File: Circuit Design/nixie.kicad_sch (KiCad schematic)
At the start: 0 parts

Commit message: all the routing is done
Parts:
- added C1, C10, C11, C12, C2, C3, C34, C35, C36, C37, C4, C5, C6, C7, C8, C9: 1uF, CoF_Capacitor:C-0402, symbol CoE_Capacitor:1uF
- added CP1, CP10, CP100, CP101, CP102, CP103, CP104, CP105, CP106, CP107, CP108, CP109, CP11, CP110, CP111, CP112, CP113, CP114, CP115, CP116, CP117, CP118, CP119, CP12, CP120, CP121, CP122, CP123, CP124, CP125, CP126, CP127, CP128, CP129, CP13, CP130, CP131, CP132, CP133, CP134, CP135, CP136, CP137, CP138, CP139, CP14, CP140, CP141, CP142, CP143, CP144, CP145, CP146, CP147, CP148, CP149, CP15, CP150, CP151, CP152, CP153, CP154, CP155, CP156, CP157, CP158, CP159, CP16, CP160, CP161, CP162, CP163, CP164, CP165, CP166, CP167, CP168, CP169, CP17, CP170, CP171, CP172, CP173, CP174, CP175, CP176, CP177, CP178, CP179, CP18, CP180, CP181, CP182, CP183, CP184, CP185, CP186, CP187, CP188, CP189, CP19, CP190, CP191, CP192, CP193, CP194, CP195, CP196, CP197, CP198, CP199, CP2, CP20, CP200, CP201, CP202, CP203, CP204, CP205, CP206, CP207, CP208, CP209, CP21, CP210, CP211, CP212, CP213, CP214, CP215, CP216, CP217, CP218, CP219, CP22, CP220, CP221, CP222, CP223, CP224, CP225, CP226, CP227, CP228, CP229, CP23, CP230, CP231, CP232, CP24, CP25, CP26, CP27, CP28, CP29, CP3, CP30, CP31, CP32, CP33, CP34, CP35, CP36, CP37, CP38, CP39, CP4, CP40, CP41, CP42, CP43, CP44, CP45, CP46, CP47, CP48, CP49, CP5, CP50, CP51, CP52, CP53, CP54, CP55, CP56, CP57, CP58, CP59, CP6, CP60, CP61, CP62, CP63, CP64, CP65, CP66, CP67, CP68, CP69, CP7, CP70, CP71, CP72, CP73, CP74, CP75, CP76, CP77, CP78, CP79, CP8, CP80, CP81, CP82, CP83, CP84, CP85, CP86, CP87, CP88, CP89, CP9, CP90, CP91, CP92, CP93, CP94, CP95, CP96, CP97, CP98, CP99: SolderPad, CoF_Connector:SolderPt_1x2mm, symbol Connector:TestPoint
- added J1: BM04B-GHS-TBT, CoF_Connector:BM04B-GHS-TBT, symbol CoE_Connector:BM04B-GHS-TBT
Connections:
- net LED Driver/CS1: now also CP169.1
- net LED Driver/CS10: now also CP115.1
- net LED Driver/CS11: now also CP109.1
- net LED Driver/CS12: now also CP103.1
- net LED Driver/CS13: now also CP97.1
- net LED Driver/CS14: now also CP91.1
- net LED Driver/CS15: now also CP85.1
- net LED Driver/CS16: now also CP79.1
- net LED Driver/CS17: now also CP73.1
- net LED Driver/CS18: now also CP67.1
- net LED Driver/CS2: now also CP163.1
- net LED Driver/CS3: now also CP157.1
- net LED Driver/CS4: now also CP151.1
- net LED Driver/CS5: now also CP145.1
- net LED Driver/CS6: now also CP139.1
- net LED Driver/CS7: now also CP133.1
- net LED Driver/CS8: now also CP127.1
- net LED Driver/CS9: now also CP121.1
- net LED Driver/SW1: now also CP1.1
- net LED Driver/SW10: now also CP55.1
- net LED Driver/SW11: now also CP61.1
- net LED Driver/SW2: now also CP7.1
- net LED Driver/SW3: now also CP13.1
- net LED Driver/SW4: now also CP19.1
- net LED Driver/SW5: now also CP25.1
- net LED Driver/SW6: now also CP31.1
- net LED Driver/SW7: now also CP37.1
- net LED Driver/SW8: now also CP43.1
- net LED Driver/SW9: now also CP49.1
- net Screen/CS1: now also CP170.1
- net Screen/CS10: now also CP116.1
- net Screen/CS11: now also CP110.1
- net Screen/CS12: now also CP104.1
- net Screen/CS13: now also CP98.1
- net Screen/CS14: now also CP92.1
- net Screen/CS15: now also CP86.1
- net Screen/CS16: now also CP80.1
- net Screen/CS17: now also CP74.1
- net Screen/CS18: now also CP68.1
- net Screen/CS2: now also CP164.1
- net Screen/CS3: now also CP158.1
- net Screen/CS4: now also CP152.1
- net Screen/CS5: now also CP146.1
- net Screen/CS6: now also CP140.1
- net Screen/CS7: now also CP134.1
- net Screen/CS8: now also CP128.1
- net Screen/CS9: now also CP122.1
- net Screen/SW1: now also CP62.1
- net Screen/SW10: now also CP8.1
- net Screen/SW11: now also CP2.1
- net Screen/SW2: now also CP56.1
- net Screen/SW3: now also CP50.1
- net Screen/SW4: now also CP44.1
- net Screen/SW5: now also CP38.1
- net Screen/SW6: now also CP32.1
- net Screen/SW7: now also CP26.1
- net Screen/SW8: now also CP20.1
- net Screen/SW9: now also CP14.1
- new net +3V3: C1.1, C10.1, C11.1, C12.1, C2.1, C3.1, C34.1, C35.1, C36.1, C37.1, C4.1, C5.1, C6.1, C7.1, C8.1, C9.1, J1.1 (Pin_1)
- new net GND: C1.2, C10.2, C11.2, C12.2, C2.2, C3.2, C34.2, C35.2, C36.2, C37.2, C4.2, C5.2, C6.2, C7.2, C8.2, C9.2, J1.4 (Pin_4), J1.MP (MountPin)
- new net LED Driver1/CS1: CP171.1
- new net LED Driver1/CS10: CP117.1
- new net LED Driver1/CS11: CP111.1
- new net LED Driver1/CS12: CP105.1
- new net LED Driver1/CS13: CP99.1
- new net LED Driver1/CS14: CP93.1
- new net LED Driver1/CS15: CP87.1
- new net LED Driver1/CS16: CP81.1
- new net LED Driver1/CS17: CP75.1
- new net LED Driver1/CS18: CP69.1
- new net LED Driver1/CS2: CP165.1
- new net LED Driver1/CS3: CP159.1
- new net LED Driver1/CS4: CP153.1
- new net LED Driver1/CS5: CP147.1
- new net LED Driver1/CS6: CP141.1
- new net LED Driver1/CS7: CP135.1
- new net LED Driver1/CS8: CP129.1
- new net LED Driver1/CS9: CP123.1
- new net LED Driver1/SW1: CP3.1
- new net LED Driver1/SW10: CP57.1
- new net LED Driver1/SW11: CP63.1
- new net LED Driver1/SW2: CP9.1
- new net LED Driver1/SW3: CP15.1
- new net LED Driver1/SW4: CP21.1
- new net LED Driver1/SW5: CP27.1
- new net LED Driver1/SW6: CP33.1
- new net LED Driver1/SW7: CP39.1
- new net LED Driver1/SW8: CP45.1
- new net LED Driver1/SW9: CP51.1
- new net LED Driver2/CS1: CP173.1
- new net LED Driver2/CS10: CP119.1
- new net LED Driver2/CS11: CP113.1
- new net LED Driver2/CS12: CP107.1
- new net LED Driver2/CS13: CP101.1
- new net LED Driver2/CS14: CP95.1
- new net LED Driver2/CS15: CP89.1
- new net LED Driver2/CS16: CP83.1
- new net LED Driver2/CS17: CP77.1
- new net LED Driver2/CS18: CP71.1
- new net LED Driver2/CS2: CP167.1
- new net LED Driver2/CS3: CP161.1
- new net LED Driver2/CS4: CP155.1
- new net LED Driver2/CS5: CP149.1
- new net LED Driver2/CS6: CP143.1
- new net LED Driver2/CS7: CP137.1
- new net LED Driver2/CS8: CP131.1
- new net LED Driver2/CS9: CP125.1
- new net LED Driver2/SW1: CP5.1
- new net LED Driver2/SW10: CP59.1
- new net LED Driver2/SW11: CP65.1
- new net LED Driver2/SW2: CP11.1
- new net LED Driver2/SW3: CP17.1
- new net LED Driver2/SW4: CP23.1
- new net LED Driver2/SW5: CP29.1
- new net LED Driver2/SW6: CP35.1
- new net LED Driver2/SW7: CP41.1
- new net LED Driver2/SW8: CP47.1
- new net LED Driver2/SW9: CP53.1
- new net LED Driver3/CS1: CP231.1
- new net LED Driver3/CS10: CP213.1
- new net LED Driver3/CS11: CP211.1
- new net LED Driver3/CS12: CP209.1
- new net LED Driver3/CS13: CP207.1
- new net LED Driver3/CS14: CP205.1
- new net LED Driver3/CS15: CP203.1
- new net LED Driver3/CS16: CP201.1
- new net LED Driver3/CS17: CP199.1
- new net LED Driver3/CS18: CP197.1
- new net LED Driver3/CS2: CP229.1
- new net LED Driver3/CS3: CP227.1
- new net LED Driver3/CS4: CP225.1
- new net LED Driver3/CS5: CP223.1
- new net LED Driver3/CS6: CP221.1
- new net LED Driver3/CS7: CP219.1
- new net LED Driver3/CS8: CP217.1
- new net LED Driver3/CS9: CP215.1
- new net LED Driver3/SW1: CP175.1
- new net LED Driver3/SW10: CP193.1
- new net LED Driver3/SW11: CP195.1
- new net LED Driver3/SW2: CP177.1
- new net LED Driver3/SW3: CP179.1
- new net LED Driver3/SW4: CP181.1
- new net LED Driver3/SW5: CP183.1
- new net LED Driver3/SW6: CP185.1
- new net LED Driver3/SW7: CP187.1
- new net LED Driver3/SW8: CP189.1
- new net LED Driver3/SW9: CP191.1
- new net SCL: J1.2 (Pin_2)
- new net SDA: J1.3 (Pin_3)
- new net Screen1/CS1: CP172.1
- new net Screen1/CS10: CP118.1
- new net Screen1/CS11: CP112.1
- new net Screen1/CS12: CP106.1
- new net Screen1/CS13: CP100.1
- new net Screen1/CS14: CP94.1
- new net Screen1/CS15: CP88.1
- new net Screen1/CS16: CP82.1
- new net Screen1/CS17: CP76.1
- new net Screen1/CS18: CP70.1
- new net Screen1/CS2: CP166.1
- new net Screen1/CS3: CP160.1
- new net Screen1/CS4: CP154.1
- new net Screen1/CS5: CP148.1
- new net Screen1/CS6: CP142.1
- new net Screen1/CS7: CP136.1
- new net Screen1/CS8: CP130.1
- new net Screen1/CS9: CP124.1
- new net Screen1/SW1: CP64.1
- new net Screen1/SW10: CP10.1
- new net Screen1/SW11: CP4.1
- new net Screen1/SW2: CP58.1
- new net Screen1/SW3: CP52.1
- new net Screen1/SW4: CP46.1
- new net Screen1/SW5: CP40.1
- new net Screen1/SW6: CP34.1
- new net Screen1/SW7: CP28.1
- new net Screen1/SW8: CP22.1
- new net Screen1/SW9: CP16.1
- new net Screen2/CS1: CP174.1
- new net Screen2/CS10: CP120.1
- new net Screen2/CS11: CP114.1
- new net Screen2/CS12: CP108.1
- new net Screen2/CS13: CP102.1
- new net Screen2/CS14: CP96.1
- new net Screen2/CS15: CP90.1
- new net Screen2/CS16: CP84.1
- new net Screen2/CS17: CP78.1
- new net Screen2/CS18: CP72.1
- new net Screen2/CS2: CP168.1
- new net Screen2/CS3: CP162.1
- new net Screen2/CS4: CP156.1
- new net Screen2/CS5: CP150.1
- new net Screen2/CS6: CP144.1
- new net Screen2/CS7: CP138.1
- new net Screen2/CS8: CP132.1
- new net Screen2/CS9: CP126.1
- new net Screen2/SW1: CP66.1
- new net Screen2/SW10: CP12.1
- new net Screen2/SW11: CP6.1
- new net Screen2/SW2: CP60.1
- new net Screen2/SW3: CP54.1
- new net Screen2/SW4: CP48.1
- new net Screen2/SW5: CP42.1
- new net Screen2/SW6: CP36.1
- new net Screen2/SW7: CP30.1
- new net Screen2/SW8: CP24.1
- new net Screen2/SW9: CP18.1
- new net Screen3/CS1: CP232.1
- new net Screen3/CS10: CP214.1
- new net Screen3/CS11: CP212.1
- new net Screen3/CS12: CP210.1
- new net Screen3/CS13: CP208.1
- new net Screen3/CS14: CP206.1
- new net Screen3/CS15: CP204.1
- new net Screen3/CS16: CP202.1
- new net Screen3/CS17: CP200.1
- new net Screen3/CS18: CP198.1
- new net Screen3/CS2: CP230.1
- new net Screen3/CS3: CP228.1
- new net Screen3/CS4: CP226.1
- new net Screen3/CS5: CP224.1
- new net Screen3/CS6: CP222.1
- new net Screen3/CS7: CP220.1
- new net Screen3/CS8: CP218.1
- new net Screen3/CS9: CP216.1
- new net Screen3/SW1: CP196.1
- new net Screen3/SW10: CP178.1
- new net Screen3/SW11: CP176.1
- new net Screen3/SW2: CP194.1
- new net Screen3/SW3: CP192.1
- new net Screen3/SW4: CP190.1
- new net Screen3/SW5: CP188.1
- new net Screen3/SW6: CP186.1
- new net Screen3/SW7: CP184.1
- new net Screen3/SW8: CP182.1
- new net Screen3/SW9: CP180.1
- no-connect marks 0 -> 4
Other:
- added sheet LED Driver1 (controller.kicad_sch)
- added sheet LED Driver2 (controller.kicad_sch)
- added sheet LED Driver3 (controller.kicad_sch)
- added sheet Screen1 (matrix.kicad_sch)
- added sheet Screen2 (matrix.kicad_sch)
- added sheet Screen3 (matrix.kicad_sch)
- sheet LED Driver ports: added ADDR1, ADDR2, SCL, SDA, SDB, SYNC; removed none

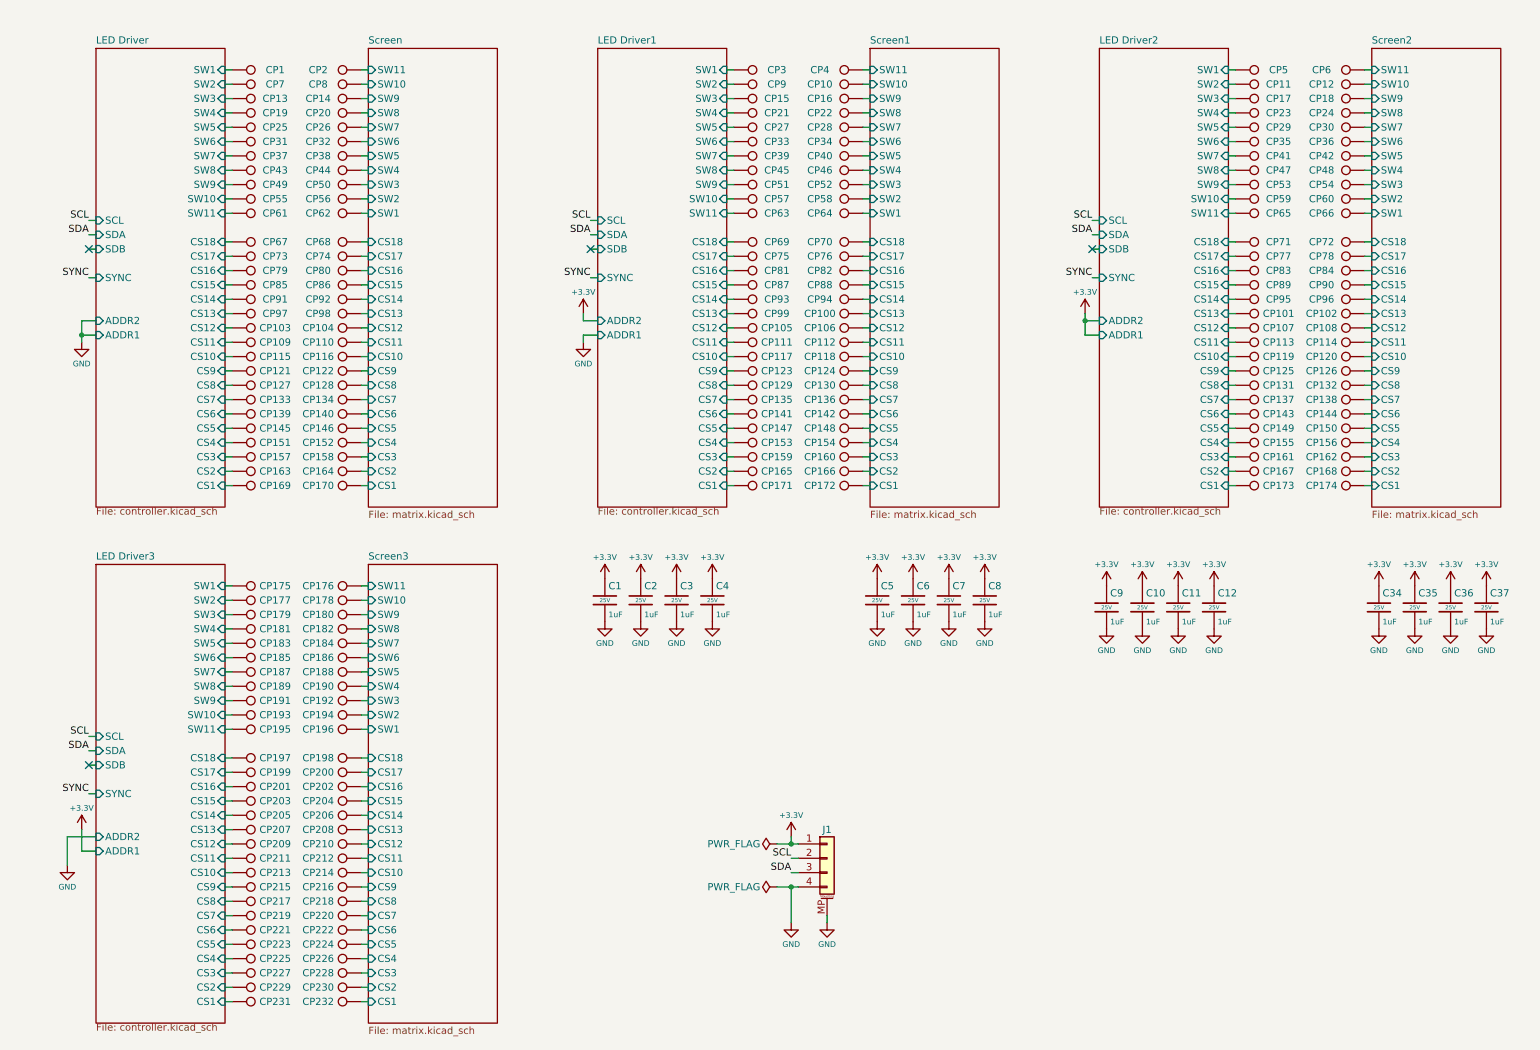
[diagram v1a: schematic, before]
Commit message: added IS31FL3731 and, edited its page
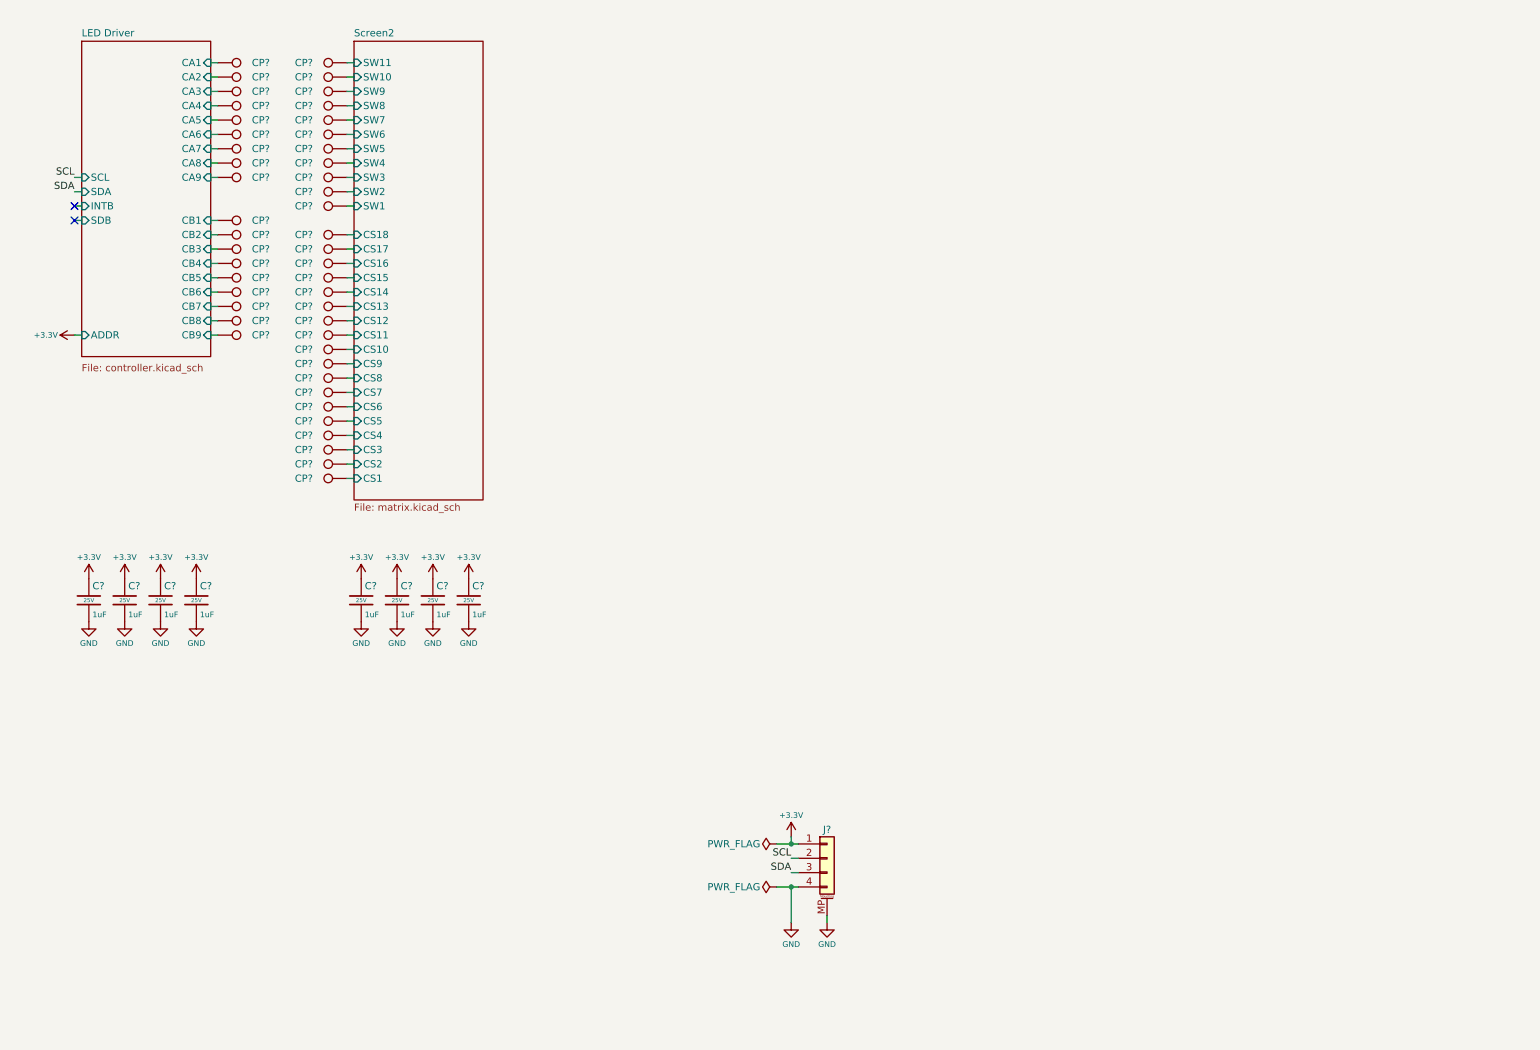
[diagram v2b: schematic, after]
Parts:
- removed C1, C2, C3, C4, C5, C6, C7, C8: 1uF, CoF_Capacitor:C-0402, symbol CoE_Capacitor:1uF
- removed CP1, CP10, CP100, CP103, CP104, CP105, CP106, CP109, CP110, CP111, CP112, CP115, CP116, CP117, CP118, CP121, CP122, CP123, CP124, CP125, CP127, CP128, CP129, CP13, CP130, CP131, CP133, CP134, CP135, CP136, CP137, CP139, CP14, CP140, CP141, CP142, CP143, CP145, CP146, CP147, CP148, CP149, CP15, CP151, CP152, CP153, CP154, CP155, CP157, CP158, CP159, CP16, CP160, CP161, CP163, CP164, CP165, CP166, CP167, CP169, CP170, CP171, CP172, CP173, CP175, CP176, CP177, CP178, CP179, CP180, CP181, CP182, CP183, CP184, CP185, CP186, CP187, CP188, CP189, CP19, CP190, CP191, CP192, CP193, CP194, CP195, CP196, CP197, CP198, CP199, CP2, CP20, CP200, CP201, CP202, CP203, CP204, CP205, CP206, CP207, CP208, CP209, CP21, CP210, CP211, CP212, CP213, CP214, CP215, CP216, CP217, CP218, CP219, CP22, CP220, CP221, CP222, CP223, CP224, CP225, CP226, CP227, CP228, CP229, CP230, CP231, CP232, CP25, CP26, CP27, CP28, CP3, CP31, CP32, CP33, CP34, CP37, CP38, CP39, CP4, CP40, CP43, CP44, CP45, CP46, CP49, CP50, CP51, CP52, CP55, CP56, CP57, CP58, CP59, CP61, CP62, CP63, CP64, CP65, CP67, CP68, CP69, CP7, CP70, CP73, CP74, CP75, CP76, CP79, CP8, CP80, CP81, CP82, CP85, CP86, CP87, CP88, CP9, CP91, CP92, CP93, CP94, CP97, CP98, CP99: SolderPad, CoF_Connector:SolderPt_1x2mm, symbol Connector:TestPoint
- renumbered C12 to C?, C11 to C?, C34 to C?, C35 to C?, C9 to C?, C10 to C?, C37 to C?, C36 to C?, CP144 to CP?, CP126 to CP?, CP71 to CP?, CP35 to CP?, CP60 to CP?, CP138 to CP?, CP23 to CP?, CP42 to CP?, CP162 to CP?, CP41 to CP?, CP113 to CP?, CP5 to CP?, CP107 to CP?, CP156 to CP?, CP54 to CP?, CP53 to CP?, CP89 to CP?, CP108 to CP?, CP95 to CP?, CP78 to CP?, CP102 to CP?, CP120 to CP?, CP90 to CP?, CP11 to CP?, CP168 to CP?, CP66 to CP?, CP29 to CP?, CP72 to CP?, CP6 to CP?, CP18 to CP?, CP150 to CP?, CP48 to CP?, CP174 to CP?, CP17 to CP?, CP36 to CP?, CP84 to CP?, CP77 to CP?, CP83 to CP?, CP132 to CP?, CP12 to CP?, CP96 to CP?, CP114 to CP?, CP47 to CP?, CP101 to CP?, CP30 to CP?, CP24 to CP?, CP119 to CP?, J1 to J?
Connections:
- net LED Driver2/CS10 renamed LED Driver/CB9
- net LED Driver2/CS11 renamed LED Driver/CB8
- net LED Driver2/CS12 renamed LED Driver/CB7
- net LED Driver2/CS13 renamed LED Driver/CB6
- net LED Driver2/CS14 renamed LED Driver/CB5
- net LED Driver2/CS15 renamed LED Driver/CB4
- net LED Driver2/CS16 renamed LED Driver/CB3
- net LED Driver2/CS17 renamed LED Driver/CB2
- net LED Driver2/CS18 renamed LED Driver/CB1
- net LED Driver2/SW1 renamed LED Driver/CA1
- net LED Driver2/SW2 renamed LED Driver/CA2
- net LED Driver2/SW3 renamed LED Driver/CA3
- net LED Driver2/SW4 renamed LED Driver/CA4
- net LED Driver2/SW5 renamed LED Driver/CA5
- net LED Driver2/SW6 renamed LED Driver/CA6
- net LED Driver2/SW7 renamed LED Driver/CA7
- net LED Driver2/SW8 renamed LED Driver/CA8
- net LED Driver2/SW9 renamed LED Driver/CA9
- no-connect marks 4 -> 2
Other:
- removed sheet LED Driver1
- removed sheet LED Driver2
- removed sheet LED Driver3
- removed sheet Screen
- removed sheet Screen1
- removed sheet Screen3
- sheet LED Driver ports: added ADDR, CA1, CA2, CA3, CA4, CA5, CA6, CA7, CA8, CA9, CB1, CB2, CB3, CB4, CB5, CB6, CB7, CB8, CB9, INTB; removed ADDR1, ADDR2, CS1, CS10, CS11, CS12, CS13, CS14, CS15, CS16, CS17, CS18, CS2, CS3, CS4, CS5, CS6, CS7, CS8, CS9, SW1, SW10, SW11, SW2, SW3, SW4, SW5, SW6, SW7, SW8, SW9, SYNC
- moved on the sheet: C?, CP?

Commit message: last commit before 0805 migration
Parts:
- removed C? (x8): 1uF, CoF_Capacitor:C-0402, symbol CoE_Capacitor:1uF
- removed CP? (x47): SolderPad, CoF_Connector:SolderPt_1x2mm, symbol Connector:TestPoint
- removed J?: BM04B-GHS-TBT, CoF_Connector:BM04B-GHS-TBT, symbol CoE_Connector:BM04B-GHS-TBT
- added BTN1: Tactile Button, CoF_Electromechanic:Tactile-5-5, symbol CoE_Electromechanic:Tactile Button
- added C1, C10, C11, C12, C13, C14, C15, C16, C19, C20, C22: 100nF, CoF_Capacitor:C-0402, symbol CoE_Capacitor:100nF
- added C17: 4.7nF, CoF_Capacitor:C-0402, symbol CoE_Capacitor:4.7nF
- added C18, C23, C24, C25, C9: 1uF, CoF_Capacitor:C-0402, symbol CoE_Capacitor:1uF
- added C2, C3, C4, C5, C6, C7, C8: 4.7uF, CoF_Capacitor:C-0402, symbol CoE_Capacitor:4.7uF
- added C21: 10nF, CoF_Capacitor:C-0402, symbol CoE_Capacitor:10nF
- added D1, D2: LED_R, CoF_Diode:LED-0603, symbol CoE_Diode:LED_R
- added J1, J2: BM04B-GHS-TBT, CoF_Connector:BM04B-GHS-TBT, symbol CoE_Connector:BM04B-GHS-TBT
- added L1: 2.2uH, CoF_Inductor:L-4-4, symbol CoE_Inductor:2.2uH
- added R1, R2: 100K, CoF_Resistor:R-0402, symbol CoE_Resistor:100K
- added R10, R11, R6, R7, R8: 22R, CoF_Resistor:R-0402, symbol CoE_Resistor:22R
- added R12, R13: 470R, CoF_Resistor:R-0402, symbol CoE_Resistor:470R
- added R14, R9: 1K, CoF_Resistor:R-0402, symbol CoE_Resistor:1K
- added R15, R16: 2K, CoF_Resistor:R-0402, symbol CoE_Resistor:2K
- added R3: 12K, CoF_Resistor:R-0402, symbol CoE_Resistor:12K
- added R4, R5: 10K, CoF_Resistor:R-0402, symbol CoE_Resistor:10K
- added S1, S2: AmbLightSns, CoF_Diode:LED-0603, symbol CoE_Sensor:AmbLightSns
- added U1: TLV62130, CoF_QuadFlat:QFN-16-EP, symbol CoE_IntegratedCircuit:TLV62130
- added U2: RP2040, CoF_QuadFlat:QFN-56-EP, symbol CoE_IntegratedCircuit:RP2040
- added U3: W25Q128JVP, CoF_SmallOutline:WSON-8-EP_6x5mm, symbol CoE_IntegratedCircuit:W25Q128JVP
- added Y1: CSTCE12M0, CoF_Crystal:CSTNE, symbol CoE_Clock:CSTCE12M0
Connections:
- net +3V3: now also C10.1, C11.1, C12.1, C13.1, C14.1, C15.1, C16.1, C21.1, C22.1, C23.1, C4.1, C5.1, C6.1, C7.1, C8.1, C9.1, J1.4 (Pin_4), L1.2, R1.1, R2.1, S1.1, S2.1, U1.14 (VOS), U2.1 (IOVDD), U2.10 (IOVDD), U2.22 (IOVDD), U2.33 (IOVDD), U2.42 (IOVDD), U2.43 (ADC_AVDD), U2.44 (VREG_VIN), U2.48 (USB_VDD), U2.49 (IOVDD), U3.8 (VCC)
- net GND: now also BTN1.1, BTN1.2, C1.2, C10.2, C11.2, C12.2, C13.2, C14.2, C15.2, C16.2, C17.1, C18.2, C19.2, C2.2, C20.2, C21.2, C22.2, C23.2, C24.2, C25.2, C3.2, C4.2, C5.2, C6.2, C7.2, C8.2, C9.2, D1.1 (K), D2.1 (K), J1.MP (MountPin), J2.4 (Pin_4), J2.MP (MountPin), R15.2, R16.2, R3.2, U1.15 (PGND), U1.16 (PGND), U1.17 (PAD), U1.6 (AGND), U1.7 (FSW), U1.8 (DEF), U2.19 (TESTEN), U2.57 (GND), U3.4 (GND), Y1.2
- new net: R6.2, U2.26 (RUN)
- new net: J1.1 (Pin_1), R12.1, U2.34 (GPIO22)
- new net: J1.2 (Pin_2), U2.2 (GPIO0)
- new net: J1.3 (Pin_3), U2.3 (GPIO1)
- new net: U2.20 (XIN), Y1.1
- new net: R9.1, Y1.3
- new net: R1.2, U1.4 (PG)
- new net: D2.2 (A), R13.2
- new net: J2.2 (Pin_2), R10.1
- new net: R10.2, U2.46 (USB_DM)
- new net: L1.1, U1.1 (SW), U1.2 (SW), U1.3 (SW)
- new net: R2.2, R5.1, U1.5 (FB)
- new net: C17.2, U1.9 (SS/TR)
- new net: R3.1, R4.1
- new net: R7.2, U2.24 (SWCLK)
- new net: D1.2 (A), R12.2
- new net: R4.2, R5.2
- new net: R14.1, U2.56 (QSPI_CSN), U3.1 (~{CS})
- new net: U2.55 (QSPI_SD1), U3.2 (DO(IO1))
- new net: U2.54 (QSPI_SD2), U3.3 (IO2)
- new net: U2.53 (QSPI_SD0), U3.5 (DI(IO0))
- new net: U2.52 (QSPI_SCLK), U3.6 (CLK)
- new net: U2.51 (QSPI_SD3), U3.7 (IO3)
- new net: R13.1, U2.37 (GPIO25)
- new net: R9.2, U2.21 (XOUT)
- new net: R8.2, U2.25 (SWD)
- new net: R11.2, U2.47 (USB_DP)
- new net: J2.3 (Pin_3), R11.1
- new net: BTN1.3, BTN1.4, R14.2
- new net +1V1: C18.1, C19.1, C20.1, U2.23 (DVDD), U2.45 (VREG_VOUT), U2.50 (DVDD)
- new net I2C0-SCL: U2.7 (GPIO5)
- new net I2C0-SDA: U2.6 (GPIO4)
- new net I2C1-SCL: U2.5 (GPIO3)
- new net I2C1-SDA: U2.4 (GPIO2)
- new net LightSense1: C24.1, R15.1, S1.2, U2.38 (GPIO26/ADC0)
- new net LightSense2: C25.1, R16.1, S2.2, U2.39 (GPIO27/ADC1)
- new net PVIN: C1.1, C2.1, C3.1, J2.1 (Pin_1), U1.10 (AVIN), U1.11 (PVIN), U1.12 (PVIN), U1.13 (EN)
- no-connect marks 2 -> 24
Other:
- removed sheet LED Driver
- removed sheet Screen2
- added sheet region1 (ControlledMatrix.kicad_sch)
- added sheet region2 (ControlledMatrix.kicad_sch)
- added sheet region3 (ControlledMatrix.kicad_sch)
- added sheet region4 (ControlledMatrix.kicad_sch)
- added sheet region5 (ControlledMatrix.kicad_sch)
- added sheet region6 (ControlledMatrix.kicad_sch)
- added sheet region7 (ControlledMatrix.kicad_sch)
- added sheet region8 (ControlledMatrix.kicad_sch)
